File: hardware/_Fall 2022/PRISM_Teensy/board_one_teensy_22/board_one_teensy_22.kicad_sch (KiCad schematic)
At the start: 12 parts, among them J1 Conn_01x04, J2 Conn_01x07, U1 Teensy4.1, U2 BNO055_Breakout, U3 MPL3115A2_Breakout

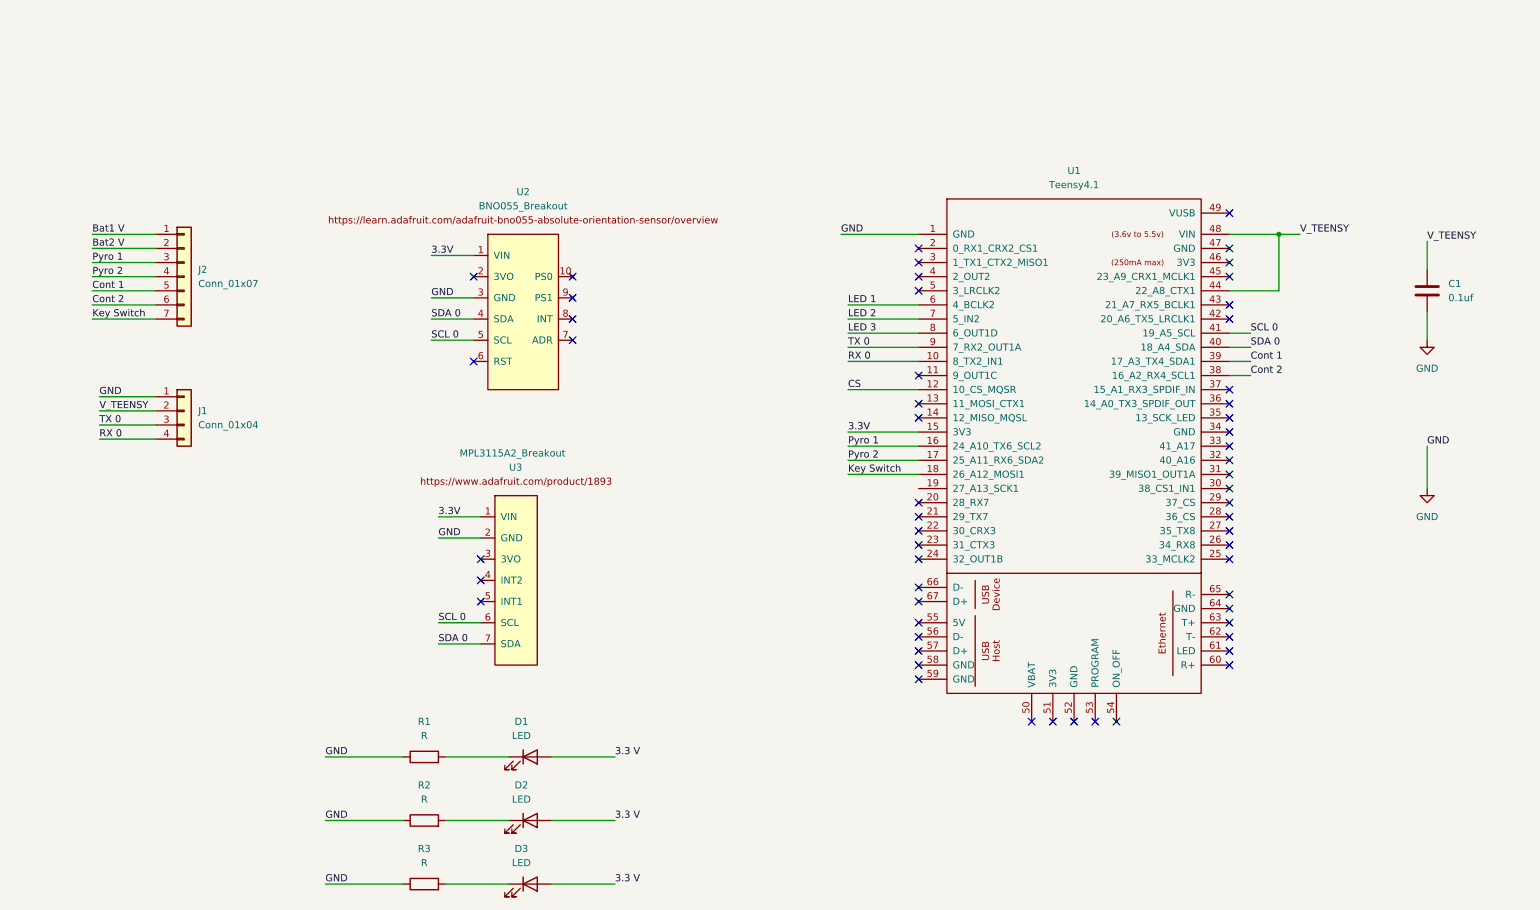
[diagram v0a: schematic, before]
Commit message: Add voltage divider for measuring battery
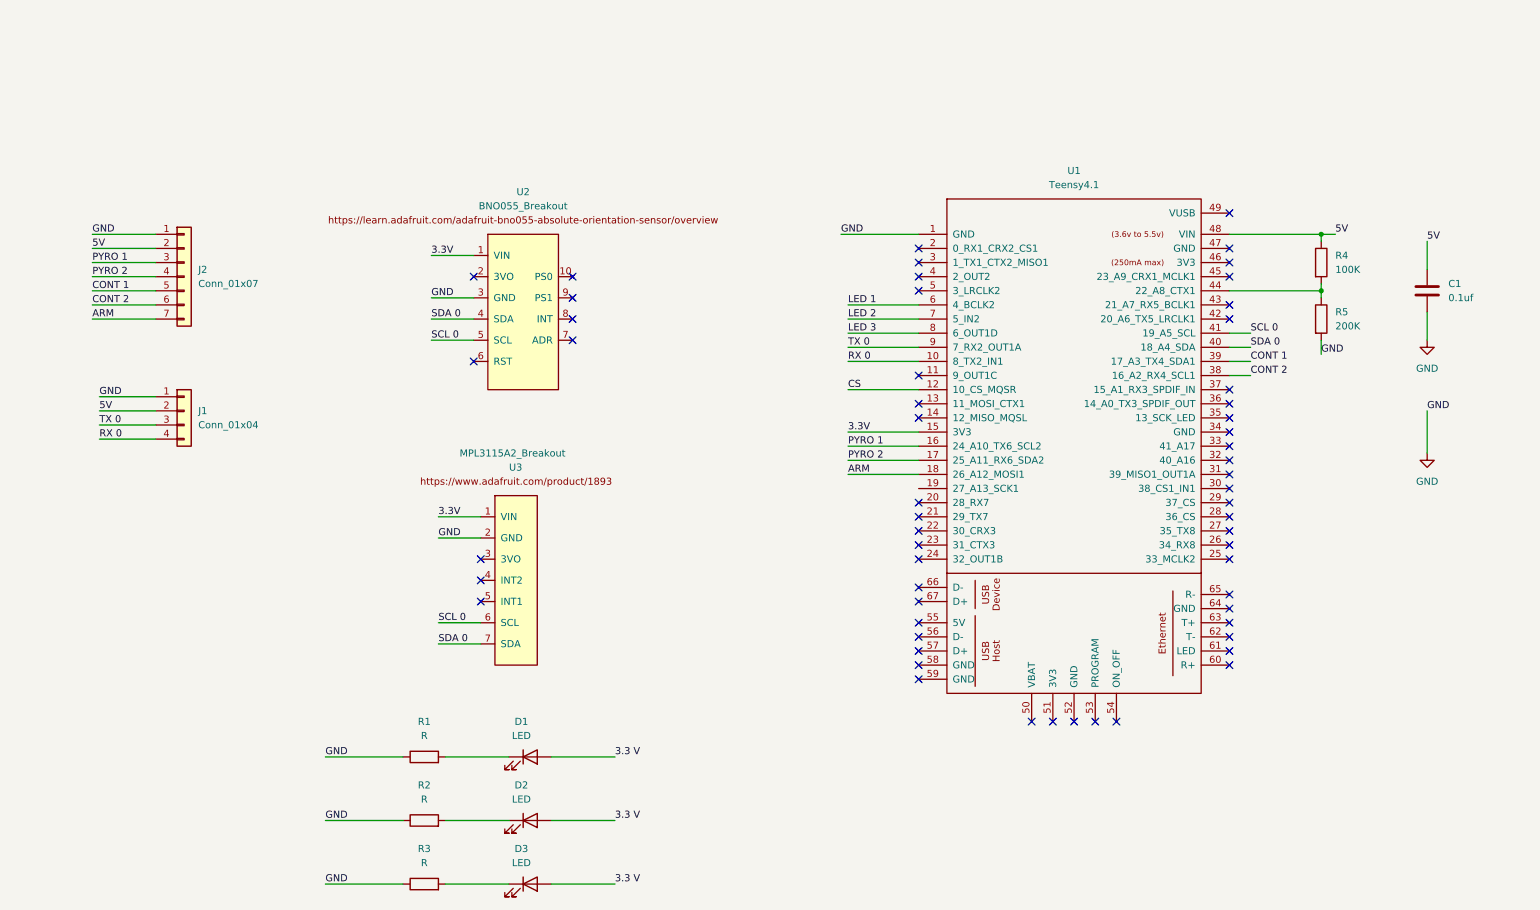
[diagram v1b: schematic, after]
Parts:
- added R4: 100K, symbol Device:R
- added R5: 200K, symbol Device:R
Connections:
- net Bat1 V is gone; now on net GND: J2.1 (Pin_1)
- net GND: now also R5.2
- net Bat2 V renamed 5V
- net 5V: now also C1.1, J1.2 (Pin_2), U1.48 (VIN), R4.1
- net Cont 1 renamed CONT 1
- net Cont 2 renamed CONT 2
- net Key Switch renamed ARM
- net Pyro 1 renamed PYRO 1
- net Pyro 2 renamed PYRO 2
- removed net V_TEENSY: C1.1, J1.2 (Pin_2), U1.44 (22_A8_CTX1), U1.48 (VIN)
- new net: R4.2, R5.1, U1.44 (22_A8_CTX1)
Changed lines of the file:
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@@
 (kicad_sch (version 20211123) (generator eeschema)
   (paper "A4")
-  (junction (at 240.03 52.07) (diameter 0) (color 0 0 0 0)
+  (junction (at 247.65 52.07) (diameter 0) (color 0 0 0 0)
+  )
+  (junction (at 247.65 62.23) (diameter 0) (color 0 0 0 0)
   )
   (no_connect (at 96.52 118.11))
@@
     (stroke (width 0) (type default) (color 0 0 0 0))
   )
+  (wire (pts (xy 247.65 52.07) (xy 247.65 53.34))
+    (stroke (width 0) (type default) (color 0 0 0 0))
+  )
   (wire (pts (xy 68.58 157.48) (xy 82.55 157.48))
     (stroke (width 0) (type default) (color 0 0 0 0))
@@
     (stroke (width 0) (type default) (color 0 0 0 0))
   )
-  (wire (pts (xy 266.7 90.17) (xy 266.7 97.79))
+  (wire (pts (xy 266.7 83.82) (xy 266.7 91.44))
     (stroke (width 0) (type default) (color 0 0 0 0))
   )
@@
     (stroke (width 0) (type default) (color 0 0 0 0))
   )
+  (wire (pts (xy 247.65 60.96) (xy 247.65 62.23))
+    (stroke (width 0) (type default) (color 0 0 0 0))
+  )
   (wire (pts (xy 109.22 157.48) (xy 120.65 157.48))
     (stroke (width 0) (type default) (color 0 0 0 0))
@@
     (stroke (width 0) (type default) (color 0 0 0 0))
   )
+  (wire (pts (xy 247.65 62.23) (xy 247.65 63.5))
+    (stroke (width 0) (type default) (color 0 0 0 0))
+  )
   (wire (pts (xy 231.14 72.39) (xy 234.95 72.39))
     (stroke (width 0) (type default) (color 0 0 0 0))
@@
     (stroke (width 0) (type default) (color 0 0 0 0))
   )
-  (wire (pts (xy 231.14 62.23) (xy 240.03 62.23))
+  (wire (pts (xy 231.14 62.23) (xy 247.65 62.23))
     (stroke (width 0) (type default) (color 0 0 0 0))
   )
@@
     (stroke (width 0) (type default) (color 0 0 0 0))
   )
-  (wire (pts (xy 240.03 52.07) (xy 243.84 52.07))
-    (stroke (width 0) (type default) (color 0 0 0 0))
-  )
   (wire (pts (xy 231.14 77.47) (xy 234.95 77.47))
     (stroke (width 0) (type default) (color 0 0 0 0))
@@
     (stroke (width 0) (type default) (color 0 0 0 0))
   )
-  (wire (pts (xy 231.14 52.07) (xy 240.03 52.07))
+  (wire (pts (xy 231.14 52.07) (xy 247.65 52.07))
     (stroke (width 0) (type default) (color 0 0 0 0))
   )
@@
     (stroke (width 0) (type default) (color 0 0 0 0))
   )
+  (wire (pts (xy 247.65 71.12) (xy 247.65 73.66))
+    (stroke (width 0) (type default) (color 0 0 0 0))
+  )
   (wire (pts (xy 162.56 74.93) (xy 175.26 74.93))
     (stroke (width 0) (type default) (color 0 0 0 0))
@@
     (stroke (width 0) (type default) (color 0 0 0 0))
   )
-  (wire (pts (xy 240.03 52.07) (xy 240.03 62.23))
-    (stroke (width 0) (type default) (color 0 0 0 0))
-  )
   (wire (pts (xy 162.56 69.85) (xy 175.26 69.85))
     (stroke (width 0) (type default) (color 0 0 0 0))
   )
+  (wire (pts (xy 247.65 52.07) (xy 250.19 52.07))
+    (stroke (width 0) (type default) (color 0 0 0 0))
+  )
   (wire (pts (xy 95.25 67.31) (xy 87.63 67.31))
     (stroke (width 0) (type default) (color 0 0 0 0))
@@
     (stroke (width 0) (type default) (color 0 0 0 0))
   )
+  (label "GND" (at 247.65 73.66 0)
+    (effects (font (size 1.27 1.27)) (justify left bottom))
+  )
   (label "3.3V" (at 87.63 55.88 0)
     (effects (font (size 1.27 1.27)) (justify left bottom))
   )
-  (label "V_TEENSY" (at 243.84 52.07 0)
+  (label "5V" (at 250.19 52.07 0)
     (effects (font (size 1.27 1.27)) (justify left bottom))
   )
@@
     (effects (font (size 1.27 1.27)) (justify left bottom))
   )
-  (label "Bat1 V" (at 26.67 52.07 0)
+  (label "GND" (at 26.67 52.07 0)
     (effects (font (size 1.27 1.27)) (justify left bottom))
   )
@@
     (effects (font (size 1.27 1.27)) (justify left bottom))
   )
-  (label "Cont 2" (at 234.95 77.47 0)
-    (effects (font (size 1.27 1.27)) (justify left bottom))
-  )
-  (label "Pyro 2" (at 26.67 59.69 0)
+  (label "CONT 2" (at 234.95 77.47 0)
+    (effects (font (size 1.27 1.27)) (justify left bottom))
+  )
+  (label "PYRO 2" (at 26.67 59.69 0)
     (effects (font (size 1.27 1.27)) (justify left bottom))
   )
@@
     (effects (font (size 1.27 1.27)) (justify left bottom))
   )
-  (label "Bat2 V" (at 26.67 54.61 0)
+  (label "5V" (at 26.67 54.61 0)
     (effects (font (size 1.27 1.27)) (justify left bottom))
   )
@@
     (effects (font (size 1.27 1.27)) (justify left bottom))
   )
-  (label "Cont 1" (at 234.95 74.93 0)
+  (label "CONT 1" (at 234.95 74.93 0)
     (effects (font (size 1.27 1.27)) (justify left bottom))
   )
@@
     (effects (font (size 1.27 1.27)) (justify left bottom))
   )
-  (label "GND" (at 266.7 90.17 0)
-    (effects (font (size 1.27 1.27)) (justify left bottom))
-  )
-  (label "Key Switch" (at 26.67 67.31 0)
-    (effects (font (size 1.27 1.27)) (justify left bottom))
-  )
-  (label "Pyro 1" (at 162.56 90.17 0)
+  (label "GND" (at 266.7 83.82 0)
+    (effects (font (size 1.27 1.27)) (justify left bottom))
+  )
+  (label "ARM" (at 26.67 67.31 0)
+    (effects (font (size 1.27 1.27)) (justify left bottom))
+  )
+  (label "PYRO 1" (at 162.56 90.17 0)
     (effects (font (size 1.27 1.27)) (justify left bottom))
   )
@@
     (effects (font (size 1.27 1.27)) (justify left bottom))
   )
-  (label "Key Switch" (at 162.56 95.25 0)
+  (label "ARM" (at 162.56 95.25 0)
     (effects (font (size 1.27 1.27)) (justify left bottom))
   )
@@
     (effects (font (size 1.27 1.27)) (justify left bottom))
   )
-  (label "V_TEENSY" (at 266.7 53.34 0)
+  (label "5V" (at 266.7 53.34 0)
     (effects (font (size 1.27 1.27)) (justify left bottom))
   )
@@
     (effects (font (size 1.27 1.27)) (justify left bottom))
   )
-  (label "Cont 2" (at 26.67 64.77 0)
+  (label "CONT 2" (at 26.67 64.77 0)
     (effects (font (size 1.27 1.27)) (justify left bottom))
   )
@@
     (effects (font (size 1.27 1.27)) (justify left bottom))
   )
-  (label "Pyro 2" (at 162.56 92.71 0)
+  (label "PYRO 2" (at 162.56 92.71 0)
     (effects (font (size 1.27 1.27)) (justify left bottom))
   )
@@
     (effects (font (size 1.27 1.27)) (justify left bottom))
   )
-  (label "Cont 1" (at 26.67 62.23 0)
+  (label "CONT 1" (at 26.67 62.23 0)
     (effects (font (size 1.27 1.27)) (justify left bottom))
   )
@@
     (effects (font (size 1.27 1.27)) (justify left bottom))
   )
-  (label "Pyro 1" (at 26.67 57.15 0)
-    (effects (font (size 1.27 1.27)) (justify left bottom))
-  )
-  (label "V_TEENSY" (at 27.94 83.82 0)
+  (label "PYRO 1" (at 26.67 57.15 0)
+    (effects (font (size 1.27 1.27)) (justify left bottom))
+  )
+  (label "5V" (at 27.94 83.82 0)
     (effects (font (size 1.27 1.27)) (justify left bottom))
   )
@@
     (pin "2")
   )
+  (symbol (lib_id "Device:R") (at 247.65 57.15 0) (unit 1)
+    (in_bom yes) (on_board yes) (fields_autoplaced)
+    (property "Reference" "R4" (id 0) (at 250.19 55.8799 0)
+      (effects (font (size 1.27 1.27)) (justify left))
+    )
+    (property "Value" "100K" (id 1) (at 250.19 58.4199 0)
+      (effects (font (size 1.27 1.27)) (justify left))
+    )
+    (property "Footprint" "" (id 2) (at 245.872 57.15 90)
+      (effects (font (size 1.27 1.27)) hide)
+    )
+    (property "Datasheet" "~" (id 3) (at 247.65 57.15 0)
+      (effects (font (size 1.27 1.27)) hide)
+    )
+    (pin "1")
+    (pin "2")
+  )
   (symbol (lib_id "Device:LED") (at 105.41 157.48 0) (unit 1)
     (in_bom yes) (on_board yes) (fields_autoplaced)
@@
     (pin "2")
   )
-  (symbol (lib_id "power:GND") (at 266.7 97.79 0) (unit 1)
-    (in_bom yes) (on_board yes) (fields_autoplaced)
-    (property "Reference" "#PWR02" (id 0) (at 266.7 104.14 0)
-      (effects (font (size 1.27 1.27)) hide)
-    )
-    (property "Value" "GND" (id 1) (at 266.7 102.87 0))
-    (property "Footprint" "" (id 2) (at 266.7 97.79 0)
-      (effects (font (size 1.27 1.27)) hide)
-    )
-    (property "Datasheet" "" (id 3) (at 266.7 97.79 0)
+  (symbol (lib_id "Device:R") (at 247.65 67.31 0) (unit 1)
+    (in_bom yes) (on_board yes) (fields_autoplaced)
+    (property "Reference" "R5" (id 0) (at 250.19 66.0399 0)
+      (effects (font (size 1.27 1.27)) (justify left))
+    )
+    (property "Value" "200K" (id 1) (at 250.19 68.5799 0)
+      (effects (font (size 1.27 1.27)) (justify left))
+    )
+    (property "Footprint" "" (id 2) (at 245.872 67.31 90)
+      (effects (font (size 1.27 1.27)) hide)
+    )
+    (property "Datasheet" "~" (id 3) (at 247.65 67.31 0)
+      (effects (font (size 1.27 1.27)) hide)
+    )
+    (pin "1")
+    (pin "2")
+  )
+  (symbol (lib_id "power:GND") (at 266.7 91.44 0) (unit 1)
+    (in_bom yes) (on_board yes) (fields_autoplaced)
+    (property "Reference" "#PWR02" (id 0) (at 266.7 97.79 0)
+      (effects (font (size 1.27 1.27)) hide)
+    )
+    (property "Value" "GND" (id 1) (at 266.7 96.52 0))
+    (property "Footprint" "" (id 2) (at 266.7 91.44 0)
+      (effects (font (size 1.27 1.27)) hide)
+    )
+    (property "Datasheet" "" (id 3) (at 266.7 91.44 0)
       (effects (font (size 1.27 1.27)) hide)
     )
@@
       (reference "R3") (unit 1) (value "R") (footprint "")
     )
+    (path "/99baa0dd-fde4-4b75-83f6-a1af8f8c4b2c"
+      (reference "R4") (unit 1) (value "100K") (footprint "")
+    )
+    (path "/b35b9880-c31b-4cfc-ab23-116f0c0cec40"
+      (reference "R5") (unit 1) (value "200K") (footprint "")
+    )
     (path "/1049841c-d8e6-470c-9b96-846caad7e784"

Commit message: Add buzzer and take out 2nd SPI
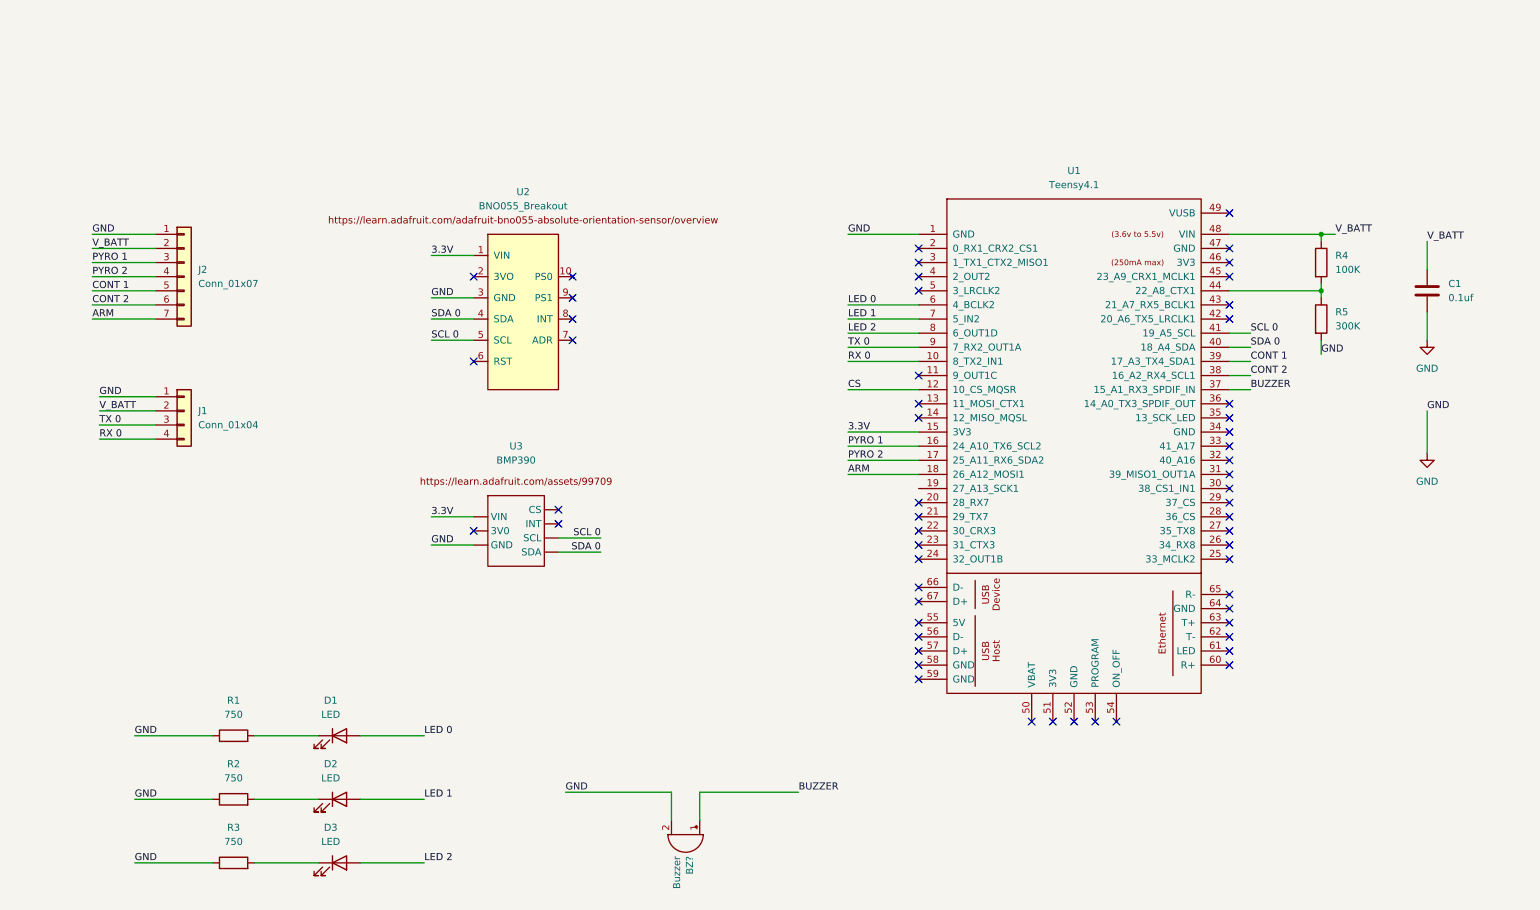
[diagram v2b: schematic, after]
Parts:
- removed U3: MPL3115A2_Breakout, sensors_2021_2022:MPL3115A2_Breakout, symbol REV2_SPRING_2022-rescue:MPL3115A2_Breakout-Sensors_2021_2022
- added BZ?: Buzzer, Olin_Rocketry:Large_Buzzer_24mmOD_14.8mmPinDistance_1.0mmPinDiameter, symbol Device:Buzzer
- added U3: BMP390, symbol Sensor:BMP3xx
- R1, R2, R3: value R -> 750
- R5: value 200K -> 300K
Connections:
- net LED 3 is gone; now on net LED 2: U1.8 (6_OUT1D)
- net 3.3V: now also U3. (VIN)
- net GND: now also BZ?.2 (+), U3. (VIN)
- net LED 1: now also D2.2 (A), U1.7 (5_IN2); no longer U1.6 (4_BCLK2)
- net LED 2: now also D3.2 (A); no longer U1.7 (5_IN2)
- net SCL 0: now also U3. (VIN)
- net SDA 0: now also U3. (VIN)
- net BUZZER: now reaches U1.37 (15_A1_RX3_SPDIF_IN)
- net BUZZER: now also BZ?.1 (-)
- removed net 3.3 V: D1.2 (A), D2.2 (A), D3.2 (A)
- net 5V renamed V_BATT
- new net LED 0: D1.2 (A), U1.6 (4_BCLK2)
- no-connect marks 58 -> 57
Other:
- moved on the sheet: D1, D2, D3, R1, R2, R3

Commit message: Add GPS EAST
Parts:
- C1: footprint (none) -> Capacitor_SMD:C_0805_2012Metric_Pad1.18x1.45mm_HandSolder
- D1, D2, D3: footprint (none) -> LED_SMD:LED_0805_2012Metric_Pad1.15x1.40mm_HandSolder
- J1: footprint (none) -> Connector_JST:JST_PH_S4B-PH-K_1x04_P2.00mm_Horizontal
- J2: footprint (none) -> Connector_JST:JST_PH_S7B-PH-K_1x07_P2.00mm_Horizontal
- R1, R2, R3: value 750 -> 150; footprint (none) -> Resistor_SMD:R_0805_2012Metric_Pad1.20x1.40mm_HandSolder
- R4, R5: footprint (none) -> Resistor_SMD:R_0805_2012Metric_Pad1.20x1.40mm_HandSolder
- U1: footprint (none) -> Teensy:Teensy41
- U2: footprint sensors_2021_2022:BNO055_Breakout -> Olin_Rocketry:BNO055
- U3: value BMP390 -> BMP388
- gave numbers to parts that had none: 1
